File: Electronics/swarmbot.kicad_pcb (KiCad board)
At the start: 2 copper layers, 100 x 180 mm, 105 parts, among them J1 12x2 JST, J2 12x2 JST, J4 Battery 1S2P, J5 Raspberry_Pi_2_3, J6 Conn_01x04_Male, J7 8P8C, Q1 BSH108, Q2 BSH108, Q3 BSH108, Q4 BSH108, Q5 RSC002P03, Q6 RSC002P03, SW1 Left, SW2 Right, SW3 SW_SPST, U1 QRE1113GR, U10 AP9101CK, U11 AP2112K-3.3, U12 INA138, U2 QRE1113GR, U3 QRE1113GR, U4 QRE1113GR, U5 QRE1113GR, U6 MPC17531A, U7 ESP32-WROOM-32D, U8 TP4056

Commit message: made some changes
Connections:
- J1 pad 20: /Left Switch Top -> unconnected-(J1-Pad20)
- J1 pad 21: /Right Switch Top -> /Left Switch Top
- J1 pad 22: unconnected-(J1-Pad22) -> /Right Switch Top
- J2 pad 20: /Left Switch Lower -> unconnected-(J2-Pad20)
- J2 pad 21: /Right Switch Lower -> /Left Switch Lower
- J2 pad 22: unconnected-(J2-Pad22) -> /Right Switch Lower
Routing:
- net /Line Sensor LEDs Lower: track 85.4 -> 146.8 mm
- net /Line Sensor 1 Lower: track 0.00 -> 58.6 mm, vias 0 -> 2
- net /Line Sensor 5 Lower: track 10.6 -> 68.8 mm, vias 1 -> 3
- net /Left Switch Lower: track 4.41 -> 60.9 mm
- net /Right Switch Lower: track 4.41 -> 51.6 mm, vias 0 -> 1
- net /Lower PCB 3V3: track 28.0 -> 30.6 mm, vias 8 -> 9

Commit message: made some changes
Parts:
- added C28: 10uF, Capacitor_SMD:C_0805_2012Metric_Pad1.18x1.45mm_HandSolder, F.Cu at (152.5, 164.5)
- added PiServo1: Conn_01x03_Male, Connector_PinHeader_2.54mm:PinHeader_1x03_P2.54mm_Vertical, F.Cu at (80.5, 154.2)
- added PiServo2: Conn_01x03_Male, Connector_PinHeader_2.54mm:PinHeader_1x03_P2.54mm_Vertical, F.Cu at (80.5, 150.0)
- J5: moved to B.Cu
- PenServo1: renamed from Servo1; moved to F.Cu
- moved C25 171.9 mm to (88.0, 128.2), turned to 180 degrees
- moved R29 168.9 mm to (118.5, 182.2)
- moved C17 159.9 mm to (152.5, 174.8), turned to -90 degrees
- moved R18 156.5 mm to (85.8, 136.5), turned to 180 degrees
- moved C26 151.8 mm to (88.0, 125.0), turned to 180 degrees
- moved C13 136.7 mm to (102.2, 146.8)
- moved R24 135.1 mm to (166.1, 160.7), turned to 90 degrees
- moved R25 129.2 mm to (160.2, 165.0)
- moved C20 128.4 mm to (144.2, 198.5)
- moved D7 126.7 mm to (159.2, 195.2)
- moved C19 125.7 mm to (134.0, 198.0)
- moved D3 125.6 mm to (158.5, 177.1), turned to 55 degrees
- moved D5 122.6 mm to (161.8, 171.7), turned to 60 degrees
- moved SW3 122.1 mm to (155.0, 182.2), turned to -135 degrees
- moved R22 121.4 mm to (157.3, 171.7)
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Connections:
- J5 pad 22: unconnected-(J5-Pad22) -> /Top PCB/RPi/PiServo2
- J5 pad 24: unconnected-(J5-Pad24) -> /Top PCB/RPi/PiServo1
- U7 pad 10: /Top PCB/ESP32/Bat V -> /H-Bridge 2B Top
- U7 pad 24: /Line Sensor 3 Top -> unconnected-(U7-Pad24)
- U7 pad 26: /Top PCB/ESP32/Line Sensor LED -> unconnected-(U7-Pad26)
- U7 pad 28: /Top PCB/ESP32/5V Switch 1 -> /Line Sensor 5 Top
- U7 pad 29: /Top PCB/ESP32/Pen Servo -> /Line Sensor 3 Top
- U7 pad 37: /Top PCB/ESP32/Bat I -> /Top PCB/ESP32/Line Sensor LED
- U7 pad 4: unconnected-(U7-Pad4) -> /Top PCB/ESP32/5V Switch 1
- U7 pad 5: unconnected-(U7-Pad5) -> /Top PCB/ESP32/Pen Servo
- U7 pad 6: /H-Bridge 2B Top -> /Top PCB/ESP32/Bat V
- U7 pad 7: /H-Bridge 2A Top -> /Top PCB/ESP32/Bat I
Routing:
- net +3V3: track 2.06 -> 94.8 mm, vias 1 -> 4
- net /Line Sensor 2 Lower: track 4.62 -> 77.3 mm
- net /Line Sensor 4 Lower: track 4.85 -> 73.9 mm
- net /Top PCB/ESP32/Flash: track 7.55 -> 70.7 mm
- net /Top PCB/ESP32/Reset: track 5.78 -> 68.3 mm
- net /Line Sensor 3 Lower: track 13.6 -> 70.9 mm, vias 1 -> 2
- net /Line Sensor LEDs Top: track 0.00 -> 50.1 mm
- net /Top PCB/Power/PowerInInrush: track 0.00 -> 48.2 mm, vias 0 -> 1
- net /Top PCB/ESP32/RX: track 19.7 -> 62.6 mm, vias 1 -> 2
- net /Top PCB/ESP32/enable: track 0.00 -> 39.9 mm, vias 0 -> 2
- net /Top PCB/ESP32/TX: track 19.1 -> 58.6 mm, vias 1 -> 2
- net /Top PCB/ESP32/Pen Servo: track 0.00 -> 39.4 mm, vias 0 -> 1
- net /Top PCB/ESP32/Bat I: track 0.00 -> 32.7 mm, vias 0 -> 2
- net /Top PCB/ESP32/Bat V: track 0.00 -> 30.4 mm, vias 0 -> 2
- net /Top PCB/ESP32/program: track 0.00 -> 26.2 mm
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- added copper zone on B.Cu, net +5V
- removed copper zone on B.Cu, net +3V3

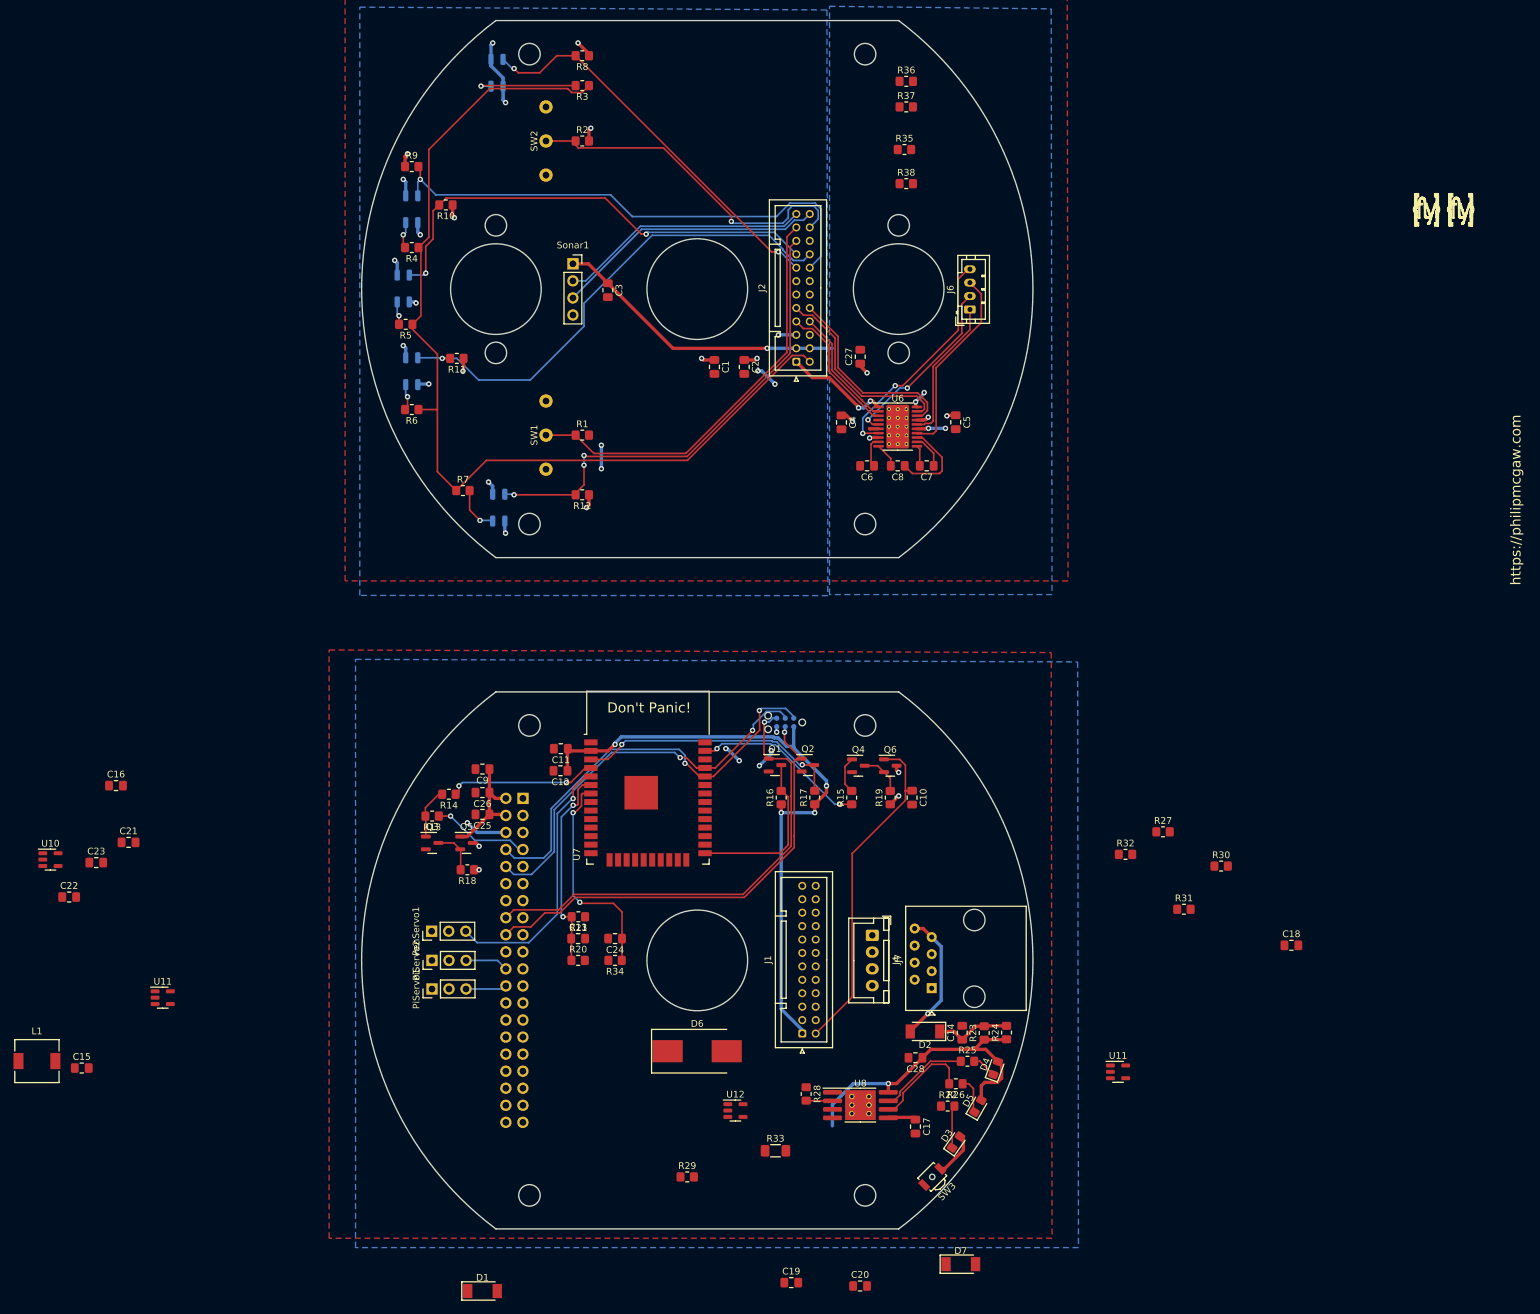
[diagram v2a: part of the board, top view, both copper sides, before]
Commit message: added bom
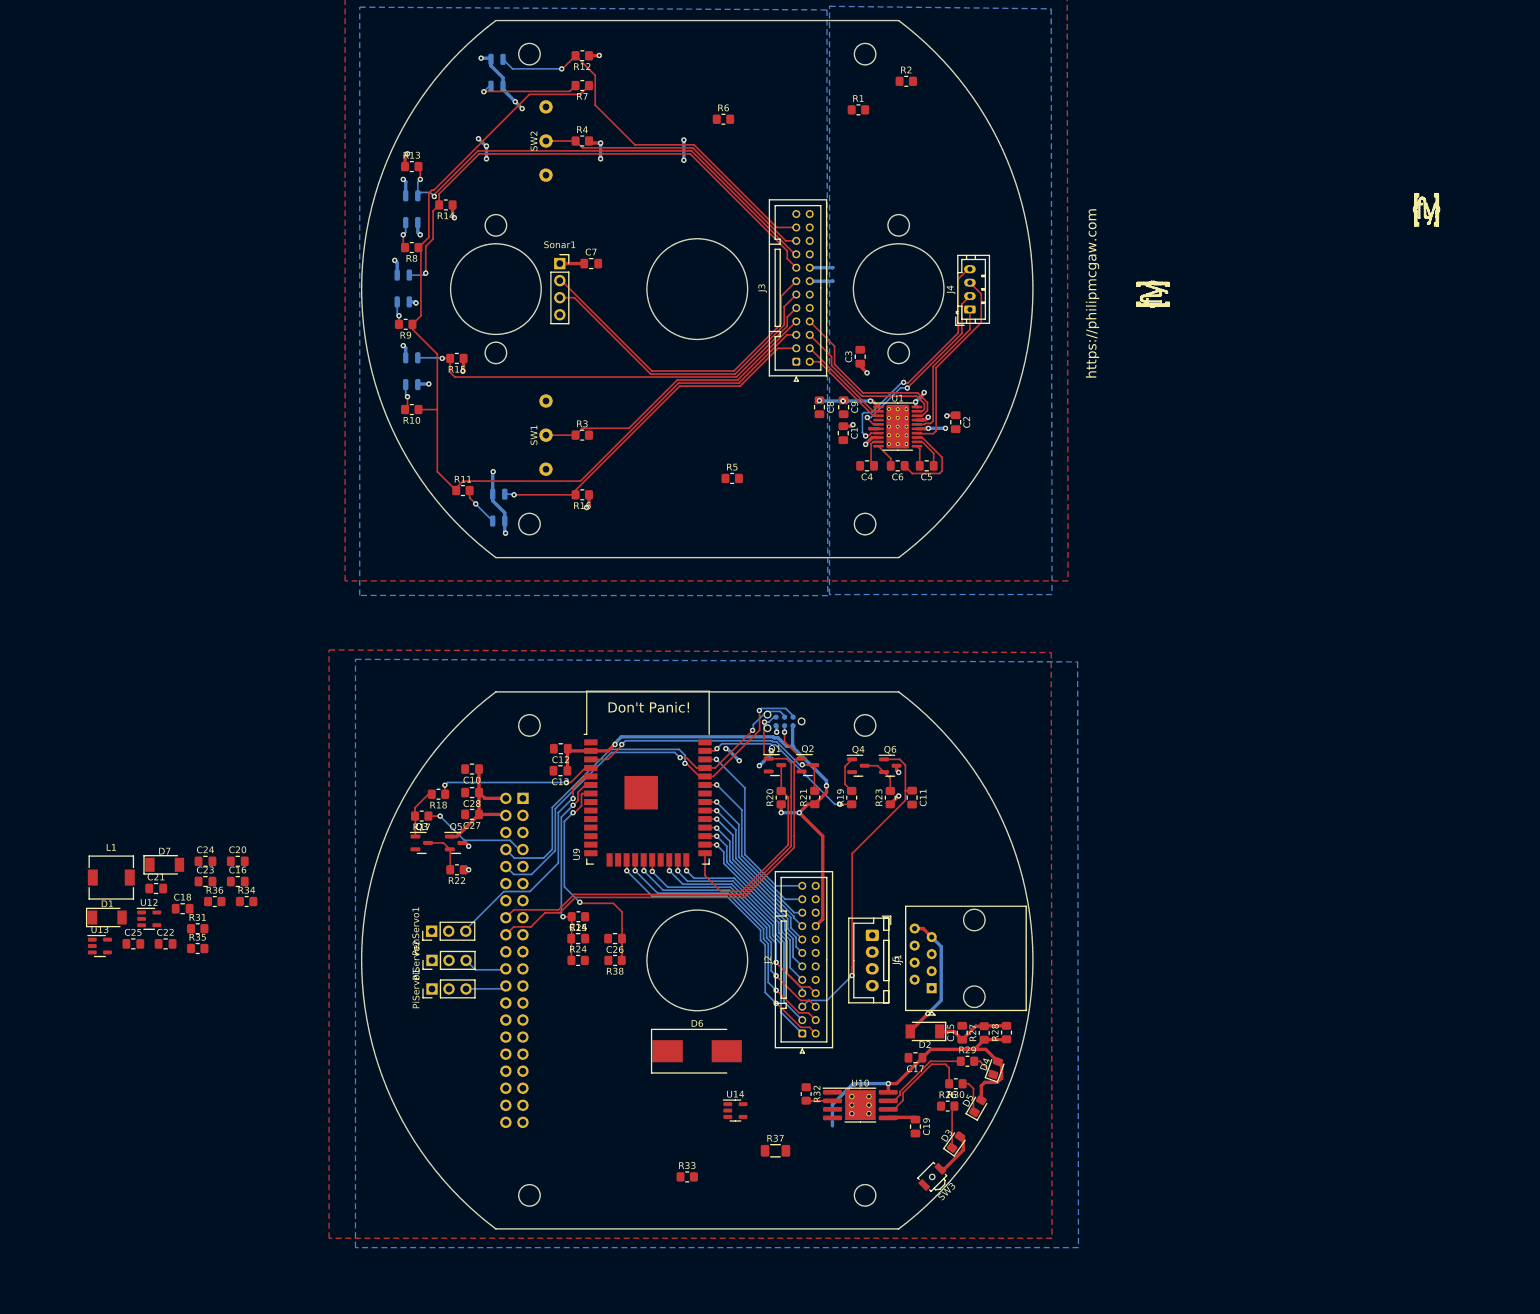
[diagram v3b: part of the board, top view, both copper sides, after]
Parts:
- removed the C15 at (28.3, 166.0)
- removed the C19 at (134.0, 198.0)
- removed the R27 at (189.4, 130.8)
- removed the R30 at (198.0, 136.0)
- removed the R32 at (183.8, 134.2)
- removed the U10 at (23.6, 135.0)
- removed U11 (x2): AP2112K-3.3, Package_TO_SOT_SMD:SOT-23-5
- added C24: 10uF, Capacitor_SMD:C_0805_2012Metric_Pad1.18x1.45mm_HandSolder, F.Cu at (46.7, 135.2)
- added C25: 1uF, Capacitor_SMD:C_0805_2012Metric_Pad1.18x1.45mm_HandSolder, F.Cu at (36.0, 147.5)
- added R34: 10k, Resistor_SMD:R_0805_2012Metric_Pad1.20x1.40mm_HandSolder, F.Cu at (52.9, 141.2)
- added R35: 2k7, Resistor_SMD:R_0805_2012Metric_Pad1.20x1.40mm_HandSolder, F.Cu at (45.6, 148.2)
- added R36: 330, Resistor_SMD:R_0805_2012Metric_Pad1.20x1.40mm_HandSolder, F.Cu at (48.1, 141.2)
- added U12: AP9101CK, Package_TO_SOT_SMD:SOT-23-5, F.Cu at (38.4, 143.8)
- added U13: AP2112K-3.3, Package_TO_SOT_SMD:SOT-23-5, F.Cu at (31.0, 147.9)
- C18: value 100nF -> 22uF
- C20: value 22uF -> 100nF
- C21: value 1uF -> 22uF
- C22: value 10uF -> 22uF
- R31: value 2k7 -> 30k
- moved C18 165.2 mm to (43.3, 142.3)
- moved R31 146.9 mm to (45.6, 145.3)
- moved D7 132.7 mm to (40.7, 135.8)
- moved C20 112.2 mm to (51.5, 135.2)
- moved D1 78.9 mm to (32.1, 143.6)
- moved R5 61.1 mm to (125.2, 78.2)
- moved Logo1 47.6 mm to (187.8, 50.8), turned to 90 degrees
- moved L1 29.5 mm to (32.7, 137.7)
- moved R6 28.9 mm to (123.9, 24.7)
- moved C16 23.1 mm to (51.5, 138.2)
- moved C8 16.8 mm to (138.2, 67.6)
- moved C23 16.5 mm to (46.7, 138.2)
- moved C22 16.0 mm to (40.8, 147.5)
- moved C9 16.0 mm to (141.8, 67.6)
- moved R1 9.05 mm to (144.0, 23.3)
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- renumbered C4 to C1, C9 to C10, C10 to C11, C11 to C12, C12 to C13, C13 to C14, C14 to C15, C28 to C17, C17 to C19, C5 to C2, C24 to C26, C25 to C27, C26 to C28, C27 to C3, C6 to C4, C7 to C5, C8 to C6, C3 to C7, C1 to C8, C2 to C9, J7 to J1, J1 to J2, J2 to J3, J6 to J4, J4 to J5, J5 to J6, R35 to R1, R6 to R10, R7 to R11, R8 to R12, R9 to R13, R10 to R14, R11 to R15, R12 to R16, R13 to R17, R14 to R18, R15 to R19, R36 to R2, R16 to R20, R17 to R21, R18 to R22, R19 to R23, R20 to R24, R21 to R25, R22 to R26, R23 to R27, R24 to R28, R25 to R29, R1 to R3, R26 to R30, R28 to R32, R29 to R33, R33 to R37, R34 to R38, R2 to R4, R37 to R5, R38 to R6, R3 to R7, R4 to R8, R5 to R9, U6 to U1, U8 to U10, U12 to U14, U1 to U4, U2 to U5, U3 to U6, U4 to U7, U5 to U8, U7 to U9
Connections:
- C18 pad 1: +BATT -> /Top PCB/Power/VBAT
- C20 pad 1: +5V -> +BATT
- C21 pad 1: /Top PCB/Power/VBAT -> +5V
- C22 pad 1: +3V3 -> +5V
- C23 pad 1: +3V3 -> /Top PCB/Power/VBAT
- C7 pad 1: /Lower PCB 5V -> /Lower PCB 3V3
- J2 pad 1: +3V3 -> /Left Motor Sensor Top
- J2 pad 10: /H-Bridge 1A Top -> GND
- J2 pad 11: unconnected-(J1-Pad11) -> /Sonar Echo Top
- J2 pad 12: unconnected-(J1-Pad12) -> GND
- J2 pad 13: /Motor Sensor 1 Top -> /Sonar Trigger Top
- J2 pad 14: /Motor Sensor 2 Top -> +5V
- J2 pad 15: /Line Sensor 1 Top -> /Line Sensor 3 Top
- J2 pad 16: /Line Sensor 2 Top -> +5V
- J2 pad 17: /Line Sensor 3 Top -> /Line Sensor 2 Top
- J2 pad 18: /Line Sensor 4 Top -> +3V3
- J2 pad 19: /Line Sensor 5 Top -> /Right Switch Top
- J2 pad 2: /Line Sensor LEDs Top -> /H-Bridge 1B Top
- J2 pad 21: /Left Switch Top -> /Line Sensor 1 Top
- J2 pad 22: /Right Switch Top -> unconnected-(J2-Pad22)
- J2 pad 23: /Sonar Trigger Top -> /Right Motor Sensor Top
- J2 pad 24: /Sonar Echo Top -> unconnected-(J2-Pad24)
- J2 pad 3: +5V -> /Line Sensor 5 Top
- J2 pad 4: +5V -> /H-Bridge 1A Top
- J2 pad 5: GND -> /Line Sensor LEDs Top
- J2 pad 6: GND -> /H-Bridge 2A Top
- J2 pad 7: /H-Bridge 1B Top -> /Left Switch Top
- J2 pad 9: /H-Bridge 2A Top -> /Line Sensor 4 Top
- J3 pad 1: /Lower PCB 3V3 -> /Left Motor Sensor Lower
- J3 pad 10: /H-Bridge 2B Lower -> /Lower PCB GND
- J3 pad 11: unconnected-(J2-Pad11) -> /Sonar Echo Lower
- J3 pad 12: unconnected-(J2-Pad12) -> /Lower PCB GND
- J3 pad 13: /Motor Sensor 1 Lower -> /Sonar Trigger Lower
- J3 pad 14: /Motor Sensor 2 Lower -> /Lower PCB 5V
- J3 pad 15: /Line Sensor 1 Lower -> /Line Sensor 3 Lower
- J3 pad 16: /Line Sensor 2 Lower -> /Lower PCB 5V
- J3 pad 17: /Line Sensor 3 Lower -> /Line Sensor 2 Lower
- J3 pad 18: /Line Sensor 4 Lower -> /Lower PCB 3V3
- J3 pad 19: /Line Sensor 5 Lower -> /Right Switch Lower
- J3 pad 2: /Line Sensor LEDs Lower -> /H-Bridge 1B Lower
- J3 pad 21: /Left Switch Lower -> /Line Sensor 1 Lower
- J3 pad 22: /Right Switch Lower -> unconnected-(J3-Pad22)
- J3 pad 23: /Sonar Trigger Lower -> /Right Motor Sensor Lower
- J3 pad 24: /Sonar Echo Lower -> unconnected-(J3-Pad24)
- J3 pad 3: /Lower PCB 5V -> /Line Sensor 5 Lower
- J3 pad 4: /Lower PCB 5V -> /H-Bridge 1A Lower
- J3 pad 5: /Lower PCB GND -> /Line Sensor LEDs Lower
- J3 pad 6: /Lower PCB GND -> /H-Bridge 2A Lower
- J3 pad 7: /H-Bridge 1B Lower -> /Left Switch Lower
- J3 pad 8: /H-Bridge 1A Lower -> /H-Bridge 2B Lower
- J3 pad 9: /H-Bridge 2A Lower -> /Line Sensor 4 Lower
- R5 pad 2: /Motor Sensor 1 Lower -> /Left Motor Sensor Lower
- R6 pad 2: /Motor Sensor 2 Lower -> /Right Motor Sensor Lower
- Sonar1 pad 1: /Lower PCB 5V -> /Lower PCB 3V3
- U9 pad 10: /H-Bridge 2B Top -> unconnected-(U9-Pad10)
- U9 pad 11: /Sonar Trigger Top -> unconnected-(U9-Pad11)
- U9 pad 12: /Sonar Echo Top -> unconnected-(U9-Pad12)
- U9 pad 13: /Right Switch Top -> unconnected-(U9-Pad13)
- U9 pad 14: /Left Switch Top -> unconnected-(U9-Pad14)
- U9 pad 16: /Line Sensor 1 Top -> unconnected-(U9-Pad16)
- U9 pad 17: unconnected-(U7-Pad17) -> /H-Bridge 1B Top
- U9 pad 18: unconnected-(U7-Pad18) -> /H-Bridge 1A Top
- U9 pad 19: unconnected-(U7-Pad19) -> /H-Bridge 2A Top
- U9 pad 20: unconnected-(U7-Pad20) -> /H-Bridge 2B Top
- U9 pad 22: unconnected-(U7-Pad22) -> /Left Motor Sensor Top
- U9 pad 23: /Line Sensor 2 Top -> /Line Sensor 5 Top
- U9 pad 24: unconnected-(U7-Pad24) -> /Left Switch Top
- U9 pad 26: unconnected-(U7-Pad26) -> /Line Sensor 4 Top
- U9 pad 27: /Line Sensor 4 Top -> /Sonar Echo Top
- U9 pad 28: /Line Sensor 5 Top -> /Sonar Trigger Top
- U9 pad 30: /Top PCB/ESP32/Port Sensor -> /Line Sensor 2 Top
- U9 pad 31: /Top PCB/ESP32/Starboard Sensor -> /Right Switch Top
- U9 pad 33: /Motor Sensor 1 Top -> /Line Sensor 1 Top
- U9 pad 36: /Motor Sensor 2 Top -> /Right Motor Sensor Top
- U9 pad 8: /H-Bridge 1A Top -> unconnected-(U9-Pad8)
- U9 pad 9: /H-Bridge 1B Top -> unconnected-(U9-Pad9)
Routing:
- net /H-Bridge 1B Top: track 0.00 -> 44.9 mm, vias 0 -> 2
- net /H-Bridge 1A Top: track 0.00 -> 42.0 mm, vias 0 -> 2
- net /H-Bridge 2A Top: track 0.00 -> 39.0 mm, vias 0 -> 2
- net /Left Motor Sensor Top: track 0.00 -> 38.3 mm, vias 0 -> 1
- net /Lower PCB 5V: track 52.2 -> 15.8 mm, vias 6 -> 5
- net /H-Bridge 2B Top: track 0.00 -> 36.2 mm, vias 0 -> 2
- net /Line Sensor 5 Top: track 0.00 -> 35.5 mm, vias 0 -> 1
- net /Left Switch Top: track 0.00 -> 30.5 mm, vias 0 -> 1
- net /Right Motor Sensor Top: track 0.00 -> 28.1 mm, vias 0 -> 1
- net /Line Sensor 4 Top: track 0.00 -> 27.1 mm, vias 0 -> 1
- net /Sonar Echo Top: track 0.00 -> 26.4 mm, vias 0 -> 1
- net /Sonar Trigger Top: track 0.00 -> 25.7 mm, vias 0 -> 1
- net /Line Sensor 1 Top: track 0.00 -> 25.6 mm, vias 0 -> 1
- net /Line Sensor 3 Top: track 0.00 -> 25.0 mm, vias 0 -> 1
- net /Line Sensor 2 Top: track 0.00 -> 24.2 mm, vias 0 -> 1
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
